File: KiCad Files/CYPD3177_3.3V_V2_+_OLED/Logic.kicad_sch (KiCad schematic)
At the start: 23 parts, among them Q1 DMC2990UDJ-7, SW1 GT-TC0060-H050-L1, SW2 B3U-1000P, U2 ATtiny1617-M, U3 TCA9406DC

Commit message: changed pcb
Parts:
- renumbered C34 to C1, C35 to C2, C22 to C3, D10 to D1, D11 to D2, R28 to R1, R37 to R10, R39 to R11, R36 to R12, R41 to R13, R29 to R2, R31 to R3, R30 to R4, R32 to R5, R34 to R6, R38 to R7, R40 to R8, R25 to R9, U3 to U1

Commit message: schematics done
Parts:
- removed U2: ATtiny1617-M, Package_DFN_QFN:QFN-24-1EP_4x4mm_P0.5mm_EP2.6x2.6mm, symbol MCU_Microchip_ATtiny:ATtiny1617-M
- added C23: 100nf, Capacitor_SMD:C_0402_1005Metric, symbol Device:C
- added J5: 0.91 OLED, test:SSD1306-0.91-OLED-4pin-128x32, symbol Connector_Generic:Conn_01x04
- added J6: QWIIC, Connector_JST:JST_SH_SM04B-SRSS-TB_1x04-1MP_P1.00mm_Horizontal, symbol Connector_Generic:Conn_01x04
- added N21: Conn_01x02_Pin, Connector_PinHeader_2.54mm:PinHeader_1x02_P2.54mm_Vertical, symbol Connector:Conn_01x02_Pin
- added R32: 10k, Resistor_SMD:R_0402_1005Metric, symbol Device:R
- added R33: R_Shunt, Inductor_SMD:L_1206_3216Metric_Pad1.42x1.75mm_HandSolder, symbol Device:R_Shunt
- added U2: INA238, Package_SO:VSSOP-10_3x3mm_P0.5mm, symbol Sensor_Energy:INA238
- added U9: ATtiny3217-M, Package_DFN_QFN:QFN-24-1EP_4x4mm_P0.5mm_EP2.6x2.6mm, symbol MCU_Microchip_ATtiny:ATtiny3217-M
- U1: footprint Package_BGA:Texas_DSBGA-8_0.9x1.9mm_Layout2x4_P0.5mm -> Library:TCA9406
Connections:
- net +3.3V: now also J6.2 (Pin_2)
- net +5V: now also C23.2, J5.1 (Pin_1), R32.1, U2.6 (VS), U9.4 (VCC)
- net Failer_EN: now also U9.10 (PB6)
- net GND: now also C23.1, J5.2 (Pin_2), J6.1 (Pin_1), U2.1 (A1), U2.2 (A0), U2.7 (GND), U9.25 (GND), U9.3 (GND)
- net LOGIC_Report: now also U9.11 (PB5)
- net LOGIC_SW: now also U9.1 (PA2)
- net LOGIC_Selection: now also U9.19 (PC2)
- net Load_Monitor_VBUS: now also U9.24 (PA1)
- net PD_Int: now also U9.18 (PC1)
- net PGOOD_Logic: now also U9.12 (PB4)
- net PowerLED_EN: now also U9.9 (PB7)
- net RX: now also U9.13 (PB3)
- net SCL: now also J5.3 (Pin_3), U2.5 (SCL), U9.16 (PB0)
- net SCL_3.3v: now also J6.3 (Pin_3), N21.2 (Pin_2)
- net SDA: now also J5.4 (Pin_4), U2.4 (SDA), U9.15 (PB1)
- net SDA_3.3v: now also J6.4 (Pin_4), N21.1 (Pin_1)
- net SW_DOWN: now also U9.7 (PA6)
- net SW_LEFT: now also U9.2 (PA3)
- net SW_PRESS: now also U9.8 (PA7)
- net SW_RIGHT: now also U9.5 (PA4)
- net SW_UP: now also U9.6 (PA5)
- net TX: now also U9.14 (PB2)
- net UPDI: now also U9.23 (~{RESET}/PA0)
- net VBUS_Fault: now also U9.17 (PC0)
- net VBUS_SW: now also U9.20 (PC3)
- new net INA_ALERT: R32.2, U2.3 (~{Alert}), U9.21 (PC4)
- new net PGOOD: U9.22 (PC5)
- new net Rail_2: R33.2, U2.9 (Vin-)
- new net Rail_2_IN: R33.1, U2.10 (Vin+), U2.8 (Vbus)
- no-connect marks 2 -> 0
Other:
- note removed: "If not need for 2nd indiacitn LED, change mosfet, but soemthing similar size"
- moved on the sheet: C1, C2, R6, U1

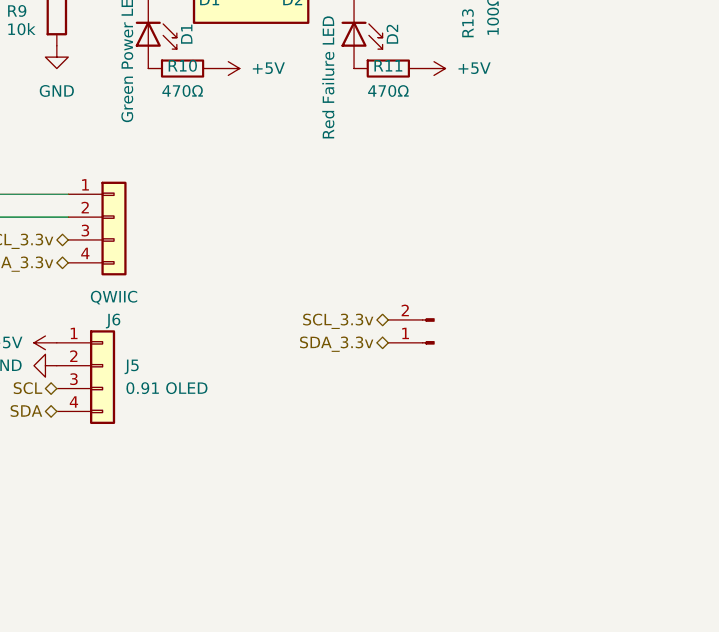
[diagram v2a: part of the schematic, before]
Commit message: major cahnges do desing, now think final design before designing pcb
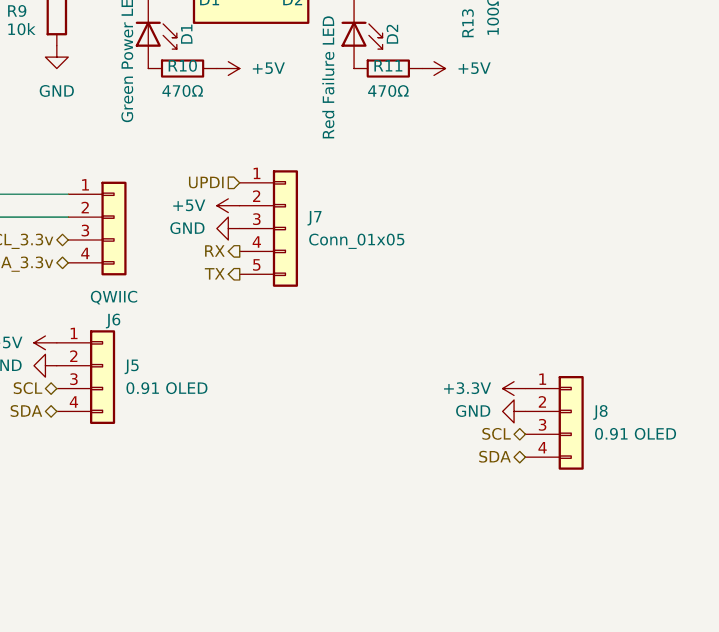
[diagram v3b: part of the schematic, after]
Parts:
- removed N21: Conn_01x02_Pin, Connector_PinHeader_2.54mm:PinHeader_1x02_P2.54mm_Vertical, symbol Connector:Conn_01x02_Pin
- added J7: Conn_01x05, Connector_PinHeader_2.54mm:PinHeader_1x05_P2.54mm_Vertical, symbol Connector_Generic:Conn_01x05
- added J8: 0.91 OLED, Connector_PinHeader_2.54mm:PinHeader_1x04_P2.54mm_Vertical, symbol Connector_Generic:Conn_01x04
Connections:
- net +3.3V: now also J8.1 (Pin_1)
- net +5V: now also J7.2 (Pin_2)
- net GND: now also J7.3 (Pin_3), J8.2 (Pin_2)
- net RX: now also J7.4 (Pin_4)
- net SCL: now also J8.3 (Pin_3)
- net SDA: now also J8.4 (Pin_4)
- net TX: now also J7.5 (Pin_5)
- net UPDI: now also J7.1 (Pin_1)

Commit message: some changes
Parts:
- C3: footprint Capacitor_SMD:C_0603_1608Metric -> Capacitor_SMD:C_0402_1005Metric_Pad0.74x0.62mm_HandSolder
- J8: value 0.91 OLED -> I2C_3.3V
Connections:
- net SCL: no longer J8.3 (Pin_3)
- net SCL_3.3v: now also J8.3 (Pin_3)
- net SDA: no longer J8.4 (Pin_4)
- net SDA_3.3v: now also J8.4 (Pin_4)
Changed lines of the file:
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@@
 			"AHQAAABvAAAAcgAAACAAAABkAAAAaQAAAGEAAABtAAAAZQAAAHQAAABlAAAAcgAAACAAAAAxAAAA"
 			"LgAAADQAAABtAAAAbQAAACwAAAAgAAAAbwAAAHUAAAB0AAAAZQAAAHIAAAAgAAAAZAAAAGkAAABh"
-			"AAAAbQAAAGUAAAB0AAAAZQAAAHIAAAAgAAAAMgAAAC4AAAA3AA=="
+			"AAAAbQAAAGUAAAB0AAAAZQAAAHIAAAAgAAAAMgAAAC4AAAA3AAAAAAAAAAAAAAAAAAAAAAAAAAAA"
+			"AAAAAAAAAAAAAAAAAAAAAAAAAAAAAAAAAAAAAAAAAAAAAAAAAAAAAAAAAAAAAAAAAAAAAAAAAAAA"
+			"AAAAAAAAAAAAAAAAAAAAAAAAAAAAAAAAAAAAAAAAAAAAAAAAAAAAAAAAAAAAAAAAAAAAAAAAAAAA"
+			"AAAAAAAAAAAAAAAAAAAAAAAAAAAAAAAAAAAAAAAAAAAAAAAAAAAAAAAAAAAAAAAAAAAAAAAAAAAA"
+			"AAAAAAAAAAAAAAAAAAAAAAAAAAAAAAAAAAAAAAAAAAAAAAAAAAAAAAAAAAAAAAAAAAAAAAAAAAAA"
+			"AAAAAAAAAAAAAAAAAAAAAAAAAAAAAAAAAAAAAAAAAAAAAAAAAAAAAAAAAAAAAAAAAAAAAAAAAAAA"
+			"AAAAAAAAAAAAAAAAAAAAAAAAAAAAAAAAAAAAAAAAAAAAAAAAAAAAAAAAAAAAAAAAAAAAAAAAAAAA"
+			"AAAAAAAAAAAAAAAAAAAAAAAAAAAAAAAAAAAAAAAAAAAAAAAAAAAAAAAAAAAAAAAAAAAAAAAAAAAA"
+			"AAAAAAAAAAAAAAAAAAAAAAAAAAAAAAAAAAAAAAAAAAAAAAAAAAAAAAAAAAAAAAAAAAAAAAAAAAAA"
+			"AAAAAAAAAAAAAAAAAAAAAAAAAAAAAAAAAAAAAAAAAAAAAAAAAAAAAAAAAAAAAAAAAAAAAAAAAAAA"
+			"AAAAAAAAAAAAAAAAAAAAAAAAAAAAAAAAAAAAAAAAAAAAAAAAAAAAAAAAAAAAAAAAAAAAAAAAAAAA"
+			"AAAAAAAAAAAAAAAAAAAAAAAAAAAAAAAAAAAAAAAAAAAAAAAAAAAAAAAAAAAAAAAAAAAAAAAAAAAA"
+			"AAAAAAAAAAAAAAAAAAAAAAAAAAAAAAAAAAAAAAAAAAAAAAAAAAAAAAAAAAAAAAAAAAAAAAAAAAAA"
+			"AAAAAAAAAAAAAAAAAAAAAAAAAAAAAAAAAAAAAAAAAAAAAAAAAAAAAAAAAAAAAAAAAAAAAAAAAAAA"
+			"AAAAAAAAAAAAAAAAAAAAAAAAAAAAAAAAAAAAAAAAAAAAAAAAAAAAAAAAAAAAAAAAAAAAAAAAAAAA"
+			"AAAAAAAAAAAAAAAAAAAAAAAAAAAAAAAAAAAAAAAAAAAAAAAAAAAAAAAAAAAAAAAAAAAAAAAAAAAA"
+			"AAAAAAAAAAAAAAAAAAAAAAAAAAAAAAAAAAAAAAAAAAAAAAAAAAAAAAAAAAAAAAAAAAAAAAAAAAAA"
+			"AAAAAAAAAAAAAAAAAAAAAAAAAAAAAAAAAAAAAAAAAAAAAAAAAAAAAAAAAAAAAAAAAAAAAAAAAAAA"
+			"AAAAAAAAAAAAAAAAAAAAAAAAAAAAAAAAAAAAAAAAAAAAAAAAAA=="
 		)
 	)
@@
 		)
 	)
-	(hierarchical_label "SDA"
-		(shape bidirectional)
-		(at 264.16 154.94 180)
-		(effects
-			(font
-				(size 1.27 1.27)
-			)
-			(justify right)
-		)
-	)
 	(hierarchical_label "VBUS_SW"
 		(shape input)
@@
 		)
 	)
+	(hierarchical_label "SCL_3.3v"
+		(shape bidirectional)
+		(at 264.16 152.4 180)
+		(effects
+			(font
+				(size 1.27 1.27)
+			)
+			(justify right)
+		)
+	)
 	(hierarchical_label "SDA"
 		(shape bidirectional)
@@
 		)
 	)
+	(hierarchical_label "SDA_3.3v"
+		(shape bidirectional)
+		(at 264.16 154.94 180)
+		(effects
+			(font
+				(size 1.27 1.27)
+			)
+			(justify right)
+		)
+	)
 	(hierarchical_label "Rail_2_IN"
 		(shape output)
@@
 		)
 	)
-	(hierarchical_label "SCL"
-		(shape bidirectional)
-		(at 264.16 152.4 180)
-		(effects
-			(font
-				(size 1.27 1.27)
-			)
-			(justify right)
-		)
-	)
 	(hierarchical_label "UPDI"
 		(shape input)
@@
 			)
 		)
-		(property "Footprint" "Capacitor_SMD:C_0603_1608Metric"
+		(property "Footprint" "Capacitor_SMD:C_0402_1005Metric_Pad0.74x0.62mm_HandSolder"
 			(at 133.35 79.0448 0)
 			(effects
@@
 			)
 		)
-		(property "Value" "0.91 OLED"
+		(property "Value" "I2C_3.3V"
 			(at 271.78 152.3999 0)
 			(effects

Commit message: changes
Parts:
- added R35, R36: 10k, Resistor_SMD:R_0402_1005Metric, symbol Device:R
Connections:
- net +5V: now also R35.1, R36.2
- net SCL: now also R35.2
- net SDA: now also R36.1

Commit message: change
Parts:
- C3: footprint Capacitor_SMD:C_0402_1005Metric_Pad0.74x0.62mm_HandSolder -> Capacitor_SMD:C_0402_1005Metric
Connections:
- net Failer_EN: now also U9.6 (PA5); no longer U9.10 (PB6)
- net LOGIC_Report: now also U9.20 (PC3); no longer U9.11 (PB5)
- net PowerLED_EN: now also U9.5 (PA4); no longer U9.9 (PB7)
- net SW_RIGHT: now also U9.9 (PB7); no longer U9.5 (PA4)
- net SW_UP: now also U9.10 (PB6); no longer U9.6 (PA5)
- net VBUS_SW: now also U9.11 (PB5); no longer U9.20 (PC3)
- net at R10.1: now also D2.2 (A); no longer D1.2 (A)
- net at Q1.3 (D2): now also D1.1 (K); no longer D2.1 (K)
- net at Q1.6 (D1): now also D2.1 (K); no longer D1.1 (K)
- net at R11.1: now also D1.2 (A); no longer D2.2 (A)
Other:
- moved on the sheet: D1, D2
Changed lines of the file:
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@@
 			"AAAAAAAAAAAAAAAAAAAAAAAAAAAAAAAAAAAAAAAAAAAAAAAAAAAAAAAAAAAAAAAAAAAAAAAAAAAA"
 			"AAAAAAAAAAAAAAAAAAAAAAAAAAAAAAAAAAAAAAAAAAAAAAAAAAAAAAAAAAAAAAAAAAAAAAAAAAAA"
+			"AAAAAAAAAAAAAAAAAAAAAAAAAAAAAAAAAAAAAAAAAAAAAAAAAAAAAAAAAAAAAAAAAAAAAAAAAAAA"
+			"AAAAAAAAAAAAAAAAAAAAAAAAAAAAAAAAAAAAAAAAAAAAAAAAAAAAAAAAAAAAAAAAAAAAAAAAAAAA"
+			"AAAAAAAAAAAAAAAAAAAAAAAAAAAAAAAAAAAAAAAAAAAAAAAAAAAAAAAAAAAAAAAAAAAAAAAAAAAA"
+			"AAAAAAAAAAAAAAAAAAAAAAAAAAAAAAAAAAAAAAAAAAAAAAAAAAAAAAAAAAAAAAAAAAAAAAAAAAAA"
+			"AAAAAAAAAAAAAAAAAAAAAAAAAAAAAAAAAAAAAAAAAAAAAAAAAAAAAAAAAAAAAAAAAAAAAAAAAAAA"
+			"AAAAAAAAAAAAAAAAAAAAAAAAAAAAAAAAAAAAAAAAAAAAAAAAAAAAAAAAAAAAAAAAAAAAAAAAAAAA"
+			"AAAAAAAAAAAAAAAAAAAAAAAAAAAAAAAAAAAAAAAAAAAAAAAAAAAAAAAAAAAAAAAAAAAAAAAAAAAA"
+			"AAAAAAAAAAAAAAAAAAAAAAAAAAAAAAAAAAAAAAAAAAAAAAAAAAAAAAAAAAAAAAAAAAAAAAAAAAAA"
+			"AAAAAAAAAAAAAAAAAAAAAAAAAAAAAAAAAAAAAAAAAAAAAAAAAAAAAAAAAAAAAAAAAAAAAAAAAAAA"
+			"AAAAAAAAAAAAAAAAAAAAAAAAAAAAAAAAAAAAAAAAAAAAAAAAAAAAAAAAAAAAAAAAAAAAAAAAAAAA"
+			"AAAAAAAAAAAAAAAAAAAAAAAAAAAAAAAAAAAAAAAAAAAAAAAAAAAAAAAAAAAAAAAAAAAAAAAAAAAA"
+			"AAAAAAAAAAAAAAAAAAAAAAAAAAAAAAAAAAAAAAAAAAAAAAAAAAAAAAAAAAAAAAAAAAAAAAAAAAAA"
+			"AAAAAAAAAAAAAAAAAAAAAAAAAAAAAAAAAAAAAAAAAAAAAAAAAAAAAAAAAAAAAAAAAAAAAAAAAAAA"
+			"AAAAAAAAAAAAAAAAAAAAAAAAAAAAAAAAAAAAAAAAAAAAAAAAAAAAAAAAAAAAAAAAAAAAAAAAAAAA"
+			"AAAAAAAAAAAAAAAAAAAAAAAAAAAAAAAAAAAAAAAAAAAAAAAAAAAAAAAAAAAAAAAAAAAAAAAAAAAA"
+			"AAAAAAAAAAAAAAAAAAAAAAAAAAAAAAAAAAAAAAAAAAAAAAAAAAAAAAAAAAAAAAAAAAAAAAAAAAAA"
+			"AAAAAAAAAAAAAAAAAAAAAAAAAAAAAAAAAAAAAAAAAAAAAAAAAAAAAAAAAAAAAAAAAAAAAAAAAAAA"
+			"AAAAAAAAAAAAAAAAAAAAAAAAAAAAAAAAAAAAAAAAAAAAAAAAAAAAAAAAAAAAAAAAAAAAAAAAAAAA"
 			"AAAAAAAAAAAAAAAAAAAAAAAAAAAAAAAAAAAAAAAAAAAAAAAAAA=="
 		)
@@
 	)
 	(label "PowerLED_EN"
-		(at 156.21 130.81 0)
+		(at 156.21 97.79 0)
 		(effects
 			(font
@@
 	)
 	(label "SW_RIGHT"
-		(at 156.21 97.79 0)
+		(at 156.21 130.81 0)
 		(effects
 			(font
@@
 	)
 	(label "Failer_EN"
-		(at 156.21 127 0)
+		(at 156.21 100.33 0)
 		(effects
 			(font
@@
 	)
 	(label "SW_UP"
-		(at 156.21 100.33 0)
+		(at 156.21 127 0)
 		(effects
 			(font
@@
 	(hierarchical_label "VBUS_SW"
 		(shape input)
-		(at 125.73 118.11 180)
+		(at 156.21 123.19 0)
 		(effects
 			(font
 				(size 1.27 1.27)
 			)
-			(justify right)
+			(justify left)
 		)
 	)
@@
 	(hierarchical_label "LOGIC_Report"
 		(shape input)
-		(at 156.21 123.19 0)
+		(at 125.73 118.11 180)
 		(effects
 			(font
 				(size 1.27 1.27)
 			)
-			(justify left)
+			(justify right)
 		)
 	)
@@
 			)
 		)
-		(property "Footprint" "Capacitor_SMD:C_0402_1005Metric_Pad0.74x0.62mm_HandSolder"
+		(property "Footprint" "Capacitor_SMD:C_0402_1005Metric"
 			(at 133.35 79.0448 0)
 			(effects
@@
 	(symbol
 		(lib_id "Custom_Parts:LED")
-		(at 222.25 109.22 270)
+		(at 245.11 109.22 270)
 		(unit 1)
 		(exclude_from_sim no)
@@
 		(dnp no)
 		(property "Reference" "D1"
-			(at 226.568 107.95 0)
+			(at 249.428 107.95 0)
 			(effects
 				(font
@@
 		)
 		(property "Value" "Green Power LED"
-			(at 219.964 110.236 0)
+			(at 242.824 110.236 0)
 			(effects
 				(font
@@
 		)
 		(property "Footprint" "LED_SMD:LED_0603_1608Metric_Pad1.05x0.95mm_HandSolder"
-			(at 226.695 109.22 0)
+			(at 249.555 109.22 0)
 			(effects
 				(font
@@
 		)
 		(property "Datasheet" "http://www.alliedelec.com/m/d/40788c34903a719969df15f1fbea1056.pdf"
-			(at 231.648 108.458 0)
+			(at 254.508 108.458 0)
 			(effects
 				(font
@@
 		)
 		(property "Description" "940nm IR-LED, 5mm"
-			(at 229.87 108.204 0)
+			(at 252.73 108.204 0)
 			(effects
 				(font
@@
 	(symbol
 		(lib_id "Custom_Parts:LED")
-		(at 245.11 109.22 270)
+		(at 222.25 109.22 270)
 		(unit 1)
 		(exclude_from_sim no)
@@
 		(dnp no)
 		(property "Reference" "D2"
-			(at 249.428 107.95 0)
+			(at 226.568 107.95 0)
 			(effects
 				(font
@@
 		)
 		(property "Value" "Red Failure LED"
-			(at 242.316 112.776 0)
+			(at 219.456 112.776 0)
 			(effects
 				(font
@@
 		)
 		(property "Footprint" "LED_SMD:LED_0603_1608Metric_Pad1.05x0.95mm_HandSolder"
-			(at 249.555 109.22 0)
+			(at 226.695 109.22 0)
 			(effects
 				(font
@@
 		)
 		(property "Datasheet" "http://www.alliedelec.com/m/d/40788c34903a719969df15f1fbea1056.pdf"
-			(at 254.508 108.458 0)
+			(at 231.648 108.458 0)
 			(effects
 				(font
@@
 		)
 		(property "Description" "940nm IR-LED, 5mm"
-			(at 252.73 108.204 0)
+			(at 229.87 108.204 0)
 			(effects
 				(font
